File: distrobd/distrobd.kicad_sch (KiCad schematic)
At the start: 91 parts, among them J1 Conn_01x01, J10 Conn_01x01, J11 Conn_01x01, J12 Conn_02x03_Odd_Even, J13 Conn_02x03_Odd_Even, J14 Conn_02x03_Odd_Even, J15 Conn_02x03_Odd_Even, J16 Conn_01x01, J17 Conn_01x01, J18 Conn_02x03_Odd_Even, J19 Conn_02x03_Odd_Even, J2 Conn_01x01, J20 Conn_01x01, J21 Conn_01x01, J22 Conn_02x03_Odd_Even, J23 Conn_02x03_Odd_Even, J24 Conn_01x01, J25 Conn_01x01, J26 Conn_02x03_Odd_Even, J27 Conn_02x03_Odd_Even, J28 Conn_01x01, J29 Conn_01x01, J3 Conn_01x14, J30 Conn_02x03_Odd_Even, J31 Conn_02x03_Odd_Even, J32 Conn_01x01, J33 Conn_01x01, J34 Conn_02x03_Odd_Even, J35 Conn_02x03_Odd_Even, J36 Conn_01x01, J37 Conn_01x01, J38 Conn_02x03_Odd_Even, J39 Conn_02x03_Odd_Even, J4 Conn_01x14, J40 Conn_01x01, J41 Conn_01x01, J42 Conn_02x03_Odd_Even, J43 Conn_02x03_Odd_Even, J44 Conn_01x01, J45 Conn_01x01, J46 Conn_01x01, J47 Conn_01x01, J48 Conn_01x01, J49 Conn_01x01, J5 Conn_01x01, J50 Conn_01x01, J51 Conn_01x01, J6 Conn_01x01, J7 Conn_01x06, J8 Conn_01x06, J9 Conn_01x08

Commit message: minor touchups
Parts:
- added J52: Conn_01x04, Connector_Harwin:Harwin_M20-89004xx_1x04_P2.54mm_Horizontal, symbol Connector_Generic:Conn_01x04
- added JP3, JP4: SolderJumper_2_Bridged, Jumper:SolderJumper-2_P1.3mm_Bridged_RoundedPad1.0x1.5mm, symbol Jumper:SolderJumper_2_Bridged
- added R1, R2, R3, R4: 4k7, Resistor_SMD:R_1206_3216Metric_Pad1.30x1.75mm_HandSolder, symbol Device:R_Small_US
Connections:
- net +5V: now also J52.3 (Pin_3)
- net DUINO_GND: now also J8.2 (Pin_2)
- net VA: now also R4.2
- net VB: now also R3.2
- net VC: now also R2.2
- net VD: now also R1.2
- net V_CGND: now also R1.1, R2.1, R3.1, R4.1
- net at J8.1 (Pin_1): now also J52.2 (Pin_2)
- net at J8.3 (Pin_3): now also JP3.2 (B)
- net at J8.4 (Pin_4): now also JP4.2 (B)
- net SDA3: now reaches J4.6 (Pin_6)
- net SDA3: now also JP4.1 (A)
- net SCL3: now reaches J4.7 (Pin_7)
- net SCL3: now also JP3.1 (A)
- no-connect marks 26 -> 22
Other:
- note added: "INTERLOCK"
- note added: "MCP4728"
- note removed: "MCP4728 analog"
- note removed: "MCP4728 digital"
- moved on the sheet: J7, J8, J9

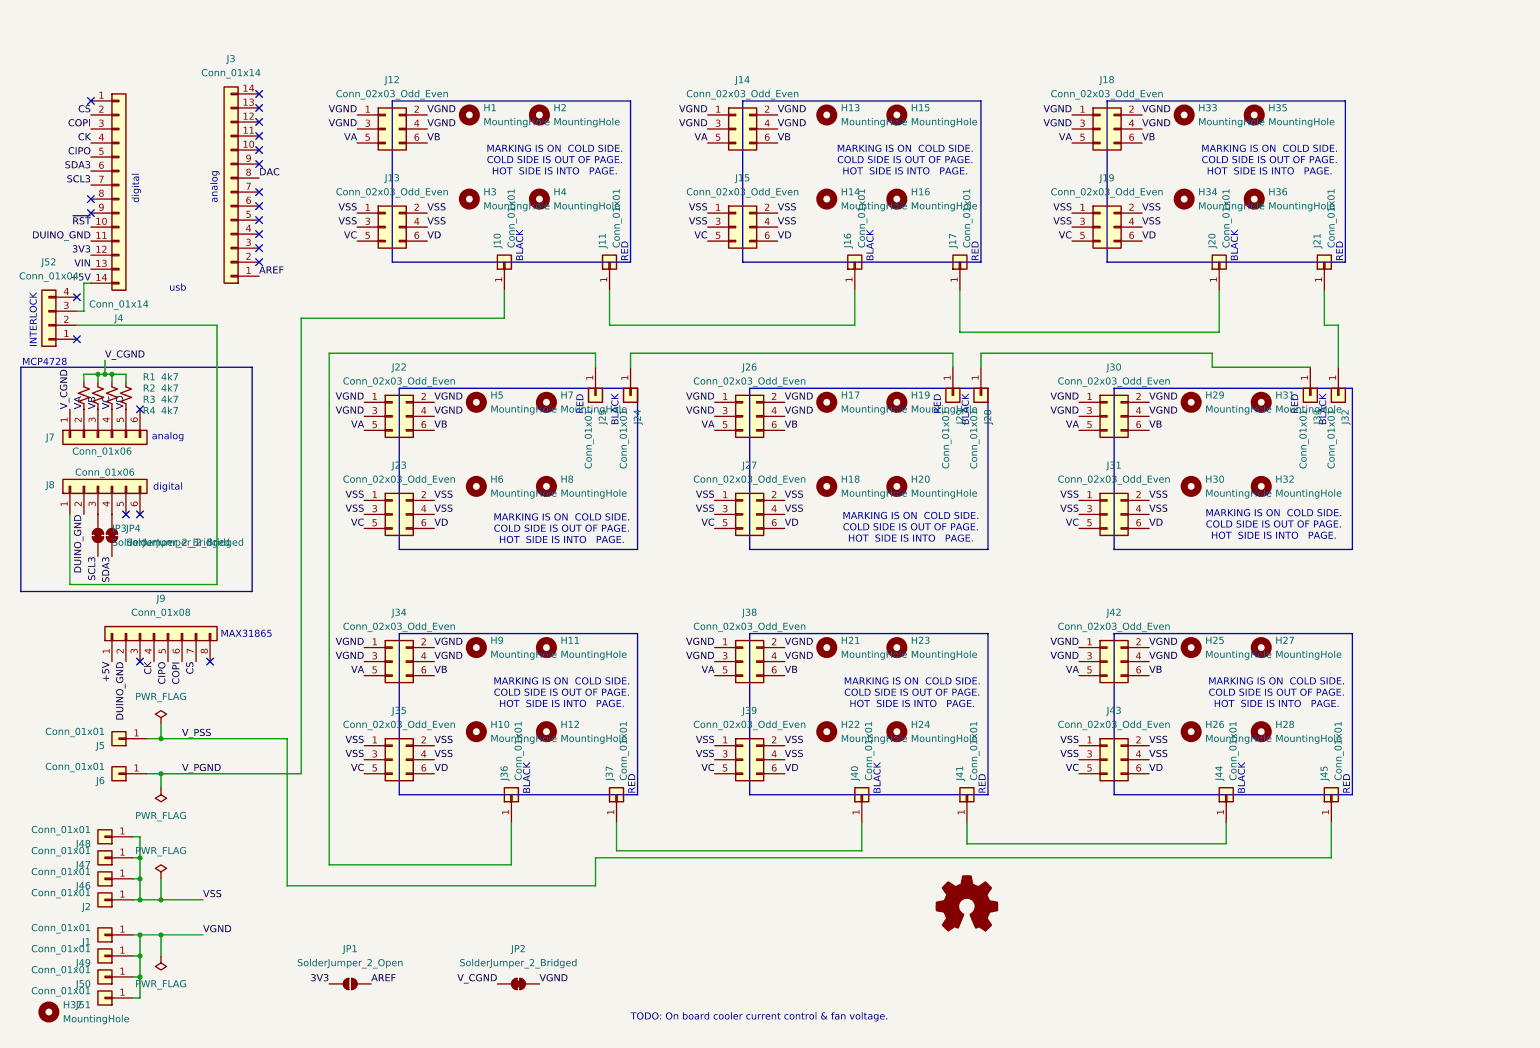
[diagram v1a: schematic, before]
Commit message: switch opamps to dual flavors, build in on-board TEC current control
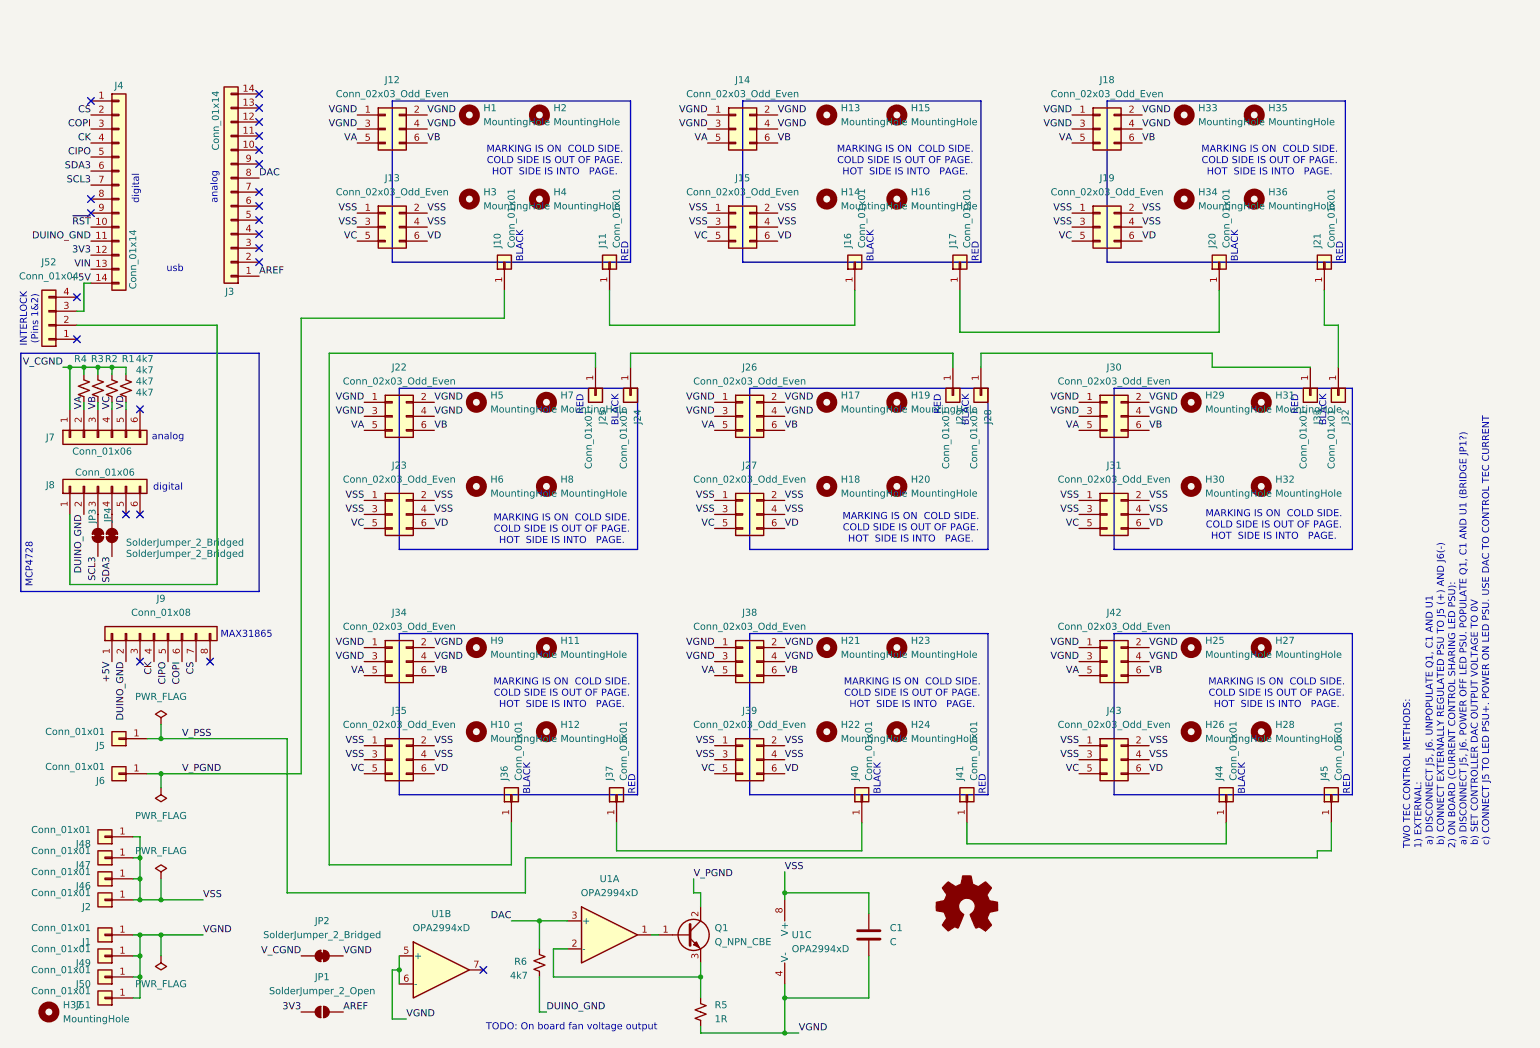
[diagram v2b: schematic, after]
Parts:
- added C1: C, Capacitor_SMD:C_0805_2012Metric_Pad1.18x1.45mm_HandSolder, symbol Device:C
- added Q1: Q_NPN_CBE, Package_TO_SOT_SMD:TO-252-2, symbol Transistor_BJT:Q_NPN_BCE
- added R5: 1R, Resistor_SMD:R_2512_6332Metric_Pad1.40x3.35mm_HandSolder, symbol Device:R_Small_US
- added R6: 4k7, Resistor_SMD:R_1206_3216Metric_Pad1.30x1.75mm_HandSolder, symbol Device:R_Small_US
- added U1: OPA2994xD, Package_SO:SOIC-8_3.9x4.9mm_P1.27mm, symbol Amplifier_Operational:OPA2994xD
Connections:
- net DAC: now also R6.1, U1.3 (+)
- net DUINO_GND: now also R6.2
- net VGND: now also C1.2, R5.2, U1.4 (V-), U1.5 (+), U1.6 (-)
- net VSS: now also C1.1, U1.8 (V+)
- net V_PGND: now also Q1.2 (C)
- new net: Q1.3 (E), R5.1, U1.2 (-)
- new net: Q1.1 (B), U1.1
- no-connect marks 22 -> 23
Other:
- note added: "INTERLOCK (Pins 1&2)"
- note added: "TODO: On board fan voltage output"
- note added: "TWO TEC CONTROL METHODS: 1) EXTERNAL: a) DISCONNECT J5, J6. UNPOPULATE Q1, C1 AND U1 b) CONNECT EXTERNALLY REGULATED PSU TO J5 (+) AND J6(-) 2) ON BOARD (CURRENT CONTROL SHARING LED PSU): a) DISCONNECT J5, J6. POWER OFF LED PSU. POPULATE Q1, C1 AND U1 (BRIDGE JP1?) b) SET CONTROLLER DAC OUTPUT VOLTAGE TO 0V c) CONNECT J5 TO LED PSU+. POWER ON LED PSU. USE DAC TO CONTROL TEC CURRENT"
- note removed: "INTERLOCK"
- note removed: "TODO: On board cooler current control & fan voltage."
- moved on the sheet: JP1, JP2, R1, R2, R3, R4

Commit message: rev up light
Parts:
- removed J46, J47, J48, J49, J50, J51, J6: Conn_01x01, custom:TE_2834012-3_1x01_P4.0mm_Horizontal, symbol Connector_Generic:Conn_01x01
- removed JP1: SolderJumper_2_Open, Jumper:SolderJumper-2_P1.3mm_Open_RoundedPad1.0x1.5mm, symbol Jumper:SolderJumper_2_Open
- removed JP2: SolderJumper_2_Bridged, Jumper:SolderJumper-2_P1.3mm_Bridged2Bar_RoundedPad1.0x1.5mm, symbol Jumper:SolderJumper_2_Bridged
- removed JP3, JP4: SolderJumper_2_Bridged, Jumper:SolderJumper-2_P1.3mm_Bridged_RoundedPad1.0x1.5mm, symbol Jumper:SolderJumper_2_Bridged
- added C2, C3: 0.1uF, Capacitor_SMD:C_0805_2012Metric_Pad1.18x1.45mm_HandSolder, symbol Device:C
- added J6: Conn_01x04, Connector_Harwin:Harwin_M20-89004xx_1x04_P2.54mm_Horizontal, symbol Connector_Generic:Conn_01x04
- added JP1, JP6, JP7, JP8: SolderJumper_2_Bridged, Jumper:SolderJumper-2_P1.3mm_Bridged2Bar_RoundedPad1.0x1.5mm, symbol Jumper:SolderJumper_2_Bridged
- added JP10, JP11, JP12, JP13, JP14, JP15, JP16, JP17, JP18, JP19, JP2, JP20, JP5, JP9: SolderJumper_2_Open, Jumper:SolderJumper-2_P1.3mm_Open_RoundedPad1.0x1.5mm, symbol Jumper:SolderJumper_2_Open
- added R10, R8: 0R, Resistor_SMD:R_1206_3216Metric_Pad1.30x1.75mm_HandSolder, symbol Device:R_Small_US
- added R7: 100K, Resistor_SMD:R_1206_3216Metric_Pad1.30x1.75mm_HandSolder, symbol Device:R_Small_US
- added U2, U3: OPA2994xD, Package_SO:SOIC-8_3.9x4.9mm_P1.27mm, symbol Amplifier_Operational:OPA2994xD
- added U4: NCS1S2412SC, Converter_DCDC:Converter_DCDC_Murata_NCS1SxxxxSC_THT, symbol Converter_DCDC:NCS1S2412SC
- C1: value C -> 0.1uF
- R5: value 1R -> 2R
- R6: value 4k7 -> 2R; footprint Resistor_SMD:R_1206_3216Metric_Pad1.30x1.75mm_HandSolder -> Resistor_SMD:R_2512_6332Metric_Pad1.40x3.35mm_HandSolder
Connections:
- net V_CGND is gone; now on net GND: J7.1 (Pin_1), R1.1, R2.1, R3.1, R4.1
- net 3V3: now also JP1.1 (A)
- net AREF: now also JP1.2 (B)
- net SCL3: now also J8.3 (Pin_3)
- net SDA3: now also J8.4 (Pin_4)
- net VA: now also JP14.2 (B), U2.1, U2.2 (-); no longer J7.2 (Pin_2), R4.2
- net VB: now also JP15.2 (B), U2.6 (-), U2.7; no longer J7.3 (Pin_3), R3.2
- net VC: now also JP16.2 (B), U3.1, U3.2 (-); no longer J7.4 (Pin_4), R2.2
- net VD: now also JP17.2 (B), U3.6 (-), U3.7; no longer J7.5 (Pin_5), R1.2
- net +5V_LOCK: now reaches J52.2 (Pin_2), J8.1 (Pin_1)
- net +5V_LOCK: now also J7.6 (Pin_6)
- net at U1.7: now also U1.6 (-), JP7.1 (A)
- net at Q1.3 (E), R5.1, U1.2 (-): now also R6.1
- net FAN_TACH: now reaches J3.13 (Pin_13)
- net FAN_TACH: now also R10.2
- net FAN_PWM: now reaches J3.14 (Pin_14)
- net FAN_PWM: now also R8.2
- removed net DAC: J3.8 (Pin_8), R6.1, U1.3 (+)
- net DUINO_GND renamed GND
- net GND: now also C1.2, J1.1 (Pin_1), J13.1 (Pin_1), J13.2 (Pin_2), J13.3 (Pin_3), J13.4 (Pin_4), J15.1 (Pin_1), J15.2 (Pin_2), J15.3 (Pin_3), J15.4 (Pin_4), J19.1 (Pin_1), J19.2 (Pin_2), J19.3 (Pin_3), J19.4 (Pin_4), J23.1 (Pin_1), J23.2 (Pin_2), J23.3 (Pin_3), J23.4 (Pin_4), J27.1 (Pin_1), J27.2 (Pin_2), J27.3 (Pin_3), J27.4 (Pin_4), J31.1 (Pin_1), J31.2 (Pin_2), J31.3 (Pin_3), J31.4 (Pin_4), J35.1 (Pin_1), J35.2 (Pin_2), J35.3 (Pin_3), J35.4 (Pin_4), J39.1 (Pin_1), J39.2 (Pin_2), J39.3 (Pin_3), J39.4 (Pin_4), J43.1 (Pin_1), J43.2 (Pin_2), J43.3 (Pin_3), J43.4 (Pin_4), R5.2, U1.4 (V-), C2.2, C3.2, JP10.2 (B), JP18.2 (B), JP2.2 (B), JP20.1 (A), JP9.2 (B), R7.1, U2.4 (V-), U3.4 (V-), U4.1 (-VIN)
- net VGND renamed VLED
- net VLED: now also J2.1 (Pin_1), C2.1, C3.1, JP11.1 (A), JP12.1 (A), JP13.1 (A), JP8.2 (B), U2.8 (V+), U3.8 (V+); no longer C1.2, J1.1 (Pin_1), R5.2, U1.4 (V-), U1.5 (+), U1.6 (-)
- removed net VSS: C1.1, J13.1 (Pin_1), J13.2 (Pin_2), J13.3 (Pin_3), J13.4 (Pin_4), J15.1 (Pin_1), J15.2 (Pin_2), J15.3 (Pin_3), J15.4 (Pin_4), J19.1 (Pin_1), J19.2 (Pin_2), J19.3 (Pin_3), J19.4 (Pin_4), J2.1 (Pin_1), J23.1 (Pin_1), J23.2 (Pin_2), J23.3 (Pin_3), J23.4 (Pin_4), J27.1 (Pin_1), J27.2 (Pin_2), J27.3 (Pin_3), J27.4 (Pin_4), J31.1 (Pin_1), J31.2 (Pin_2), J31.3 (Pin_3), J31.4 (Pin_4), J35.1 (Pin_1), J35.2 (Pin_2), J35.3 (Pin_3), J35.4 (Pin_4), J39.1 (Pin_1), J39.2 (Pin_2), J39.3 (Pin_3), J39.4 (Pin_4), J43.1 (Pin_1), J43.2 (Pin_2), J43.3 (Pin_3), J43.4 (Pin_4), U1.8 (V+)
- net V_PGND renamed VTEC_LO
- net VTEC_LO: now also JP10.1 (A), JP2.1 (A), JP9.1 (A)
- net V_PSS renamed VTEC
- net VTEC: now also C1.1, U1.8 (V+), JP11.2 (B), JP12.2 (B), JP13.2 (B), JP19.2 (B)
- new net: J6.3 (Pin_3), R10.1
- new net: J6.4 (Pin_4), R8.1
- new net: JP5.1 (A), JP7.2 (B), U1.3 (+)
- new net: JP19.1 (A), JP8.1 (A), U4.2 (+VIN)
- new net: JP18.1 (A), JP6.2 (B), U1.5 (+)
- new net 12V_FAN_POWER: J6.2 (Pin_2), U4.6 (+VOUT)
- new net FAN_GND: J6.1 (Pin_1), JP20.2 (B), U4.7 (-VOUT)
- new net TEC_DAC: J3.8 (Pin_8), JP5.2 (B), JP6.1 (A), R7.2
- new net VAR: J7.2 (Pin_2), JP14.1 (A), R4.2, U2.3 (+)
- new net VBR: J7.3 (Pin_3), JP15.1 (A), R3.2, U2.5 (+)
- new net VCR: J7.4 (Pin_4), JP16.1 (A), R2.2, U3.3 (+)
- new net VDR: J7.5 (Pin_5), JP17.1 (A), R1.2, U3.5 (+)
- no-connect marks 23 -> 22
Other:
- note added: "BRIDGE THESE TO USE LED POWER FOR TEC"
- note added: "H7 USB HERE (for upside-down mount)"
- note added: "INTERLOCK (Pins 2&3)"
- note added: "TEC SUPPLY OPTIONS: 1) EXTERNAL CONTROL: a) DNP U1, Q1, R5/R6, C1 (UNBRIDGE J1) b) BRIDGE JP2, JP9, JP10 c) UNBRIDGE, JP11, JP12, JP13 d) CONNECT EXTERNALLY REGULATED TEC PSU TO J5 (+) AND J1(-) 2) ON-BOARD CONTROL: a) SEPARATE TEC AND LED VOLTAGE SOURCES I) POPULATE U1, Q1, C1, R5/R6, BRIDGE J1 II) UNBRIDGE JP2, JP9, JP10 III) UNBRIDGE, JP11, JP12, JP13 IV) CONNECT TEC VOLTAGE SOURCE TO J5 (+) A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"
- note removed: "INTERLOCK (Pins 1&2)"
- note removed: "TODO: On board fan voltage output"
- note removed: "TWO TEC CONTROL METHODS: 1) EXTERNAL: a) DISCONNECT J5, J6. UNPOPULATE Q1, C1 AND U1 b) CONNECT EXTERNALLY REGULATED PSU TO J5 (+) AND J6(-) 2) ON BOARD (CURRENT CONTROL SHARING LED PSU): a) DISCONNECT J5, J6. POWER OFF LED PSU. POPULATE Q1, C1 AND U1 (BRIDGE JP1?) b) SET CONTROLLER DAC OUTPUT VOLTAGE TO 0V c) CONNECT J5 TO LED PSU+. POWER ON LED PSU. USE DAC TO CONTROL TEC CURRENT"
- note removed: "usb"
- moved on the sheet: C1, H37, J1, J2, J3, J4, J5, J52, J7, J8, J9, Q1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

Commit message: rev up light
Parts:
- removed J3, J4: Conn_01x14, Connector_PinSocket_2.54mm:PinSocket_1x14_P2.54mm_Vertical_SMD_Pin1Left, symbol Connector_Generic:Conn_01x14
- added H38, H39: MountingHole, MountingHole:MountingHole_2.2mm_M2, symbol Mechanical:MountingHole
- added H40, H41, H42, H43: MountingHole, custom:13.5mm_NPTH, symbol Mechanical:MountingHole
- added J46, J47: Conn_02x14_Top_Bottom, Connector_PinSocket_2.54mm:PinSocket_2x14_P2.54mm_Vertical_SMD, symbol Connector_Generic:Conn_02x14_Odd_Even
- J1, J2, J5: footprint custom:TE_2834012-3_1x01_P4.0mm_Horizontal -> custom:LF994006
- J6: footprint Connector_Harwin:Harwin_M20-89004xx_1x04_P2.54mm_Horizontal -> Connector:FanPinHeader_1x04_P2.54mm_Vertical
- JP1, JP6, JP7: footprint Jumper:SolderJumper-2_P1.3mm_Bridged2Bar_RoundedPad1.0x1.5mm -> Jumper:SolderJumper-2_P1.3mm_Bridged_RoundedPad1.0x1.5mm
- R6: footprint Resistor_SMD:R_2512_6332Metric_Pad1.40x3.35mm_HandSolder -> Package_TO_SOT_SMD:TO-263-2_TabPin1
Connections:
- net +5V: now also J46.27 (Pin_27), J46.28 (Pin_28)
- net 3V3: now also J46.23 (Pin_23), J46.24 (Pin_24)
- net AREF: now also J47.1 (Pin_1), J47.2 (Pin_2)
- net CIPO: now also J46.10 (Pin_10), J46.9 (Pin_9)
- net CK: now also J46.7 (Pin_7), J46.8 (Pin_8)
- net COPI: now also J46.5 (Pin_5), J46.6 (Pin_6)
- net CS: now also J46.3 (Pin_3), J46.4 (Pin_4)
- net FAN_PWM: now also J47.27 (Pin_27), J47.28 (Pin_28)
- net FAN_TACH: now also J47.25 (Pin_25), J47.26 (Pin_26)
- net GND: now also J46.21 (Pin_21), J46.22 (Pin_22)
- net SCL3: now also J46.13 (Pin_13), J46.14 (Pin_14)
- net SDA3: now also J46.11 (Pin_11), J46.12 (Pin_12)
- net TEC_DAC: now also J47.15 (Pin_15), J47.16 (Pin_16)
- net VIN: now also J46.25 (Pin_25), J46.26 (Pin_26)
- net ~{RST}: now also J46.19 (Pin_19), J46.20 (Pin_20)
- new net: J46.1 (Pin_1), J46.2 (Pin_2)
- new net: J46.15 (Pin_15), J46.16 (Pin_16)
- new net: J46.17 (Pin_17), J46.18 (Pin_18)
- new net: J47.10 (Pin_10), J47.9 (Pin_9)
- new net: J47.11 (Pin_11), J47.12 (Pin_12)
- new net: J47.13 (Pin_13), J47.14 (Pin_14)
- new net: J47.17 (Pin_17), J47.18 (Pin_18)
- new net: J47.19 (Pin_19), J47.20 (Pin_20)
- new net: J47.21 (Pin_21), J47.22 (Pin_22)
- new net: J47.23 (Pin_23), J47.24 (Pin_24)
- new net: J47.3 (Pin_3), J47.4 (Pin_4)
- new net: J47.5 (Pin_5), J47.6 (Pin_6)
- new net: J47.7 (Pin_7), J47.8 (Pin_8)
- no-connect marks 22 -> 7
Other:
- moved on the sheet: J9, JP19, JP20, JP8, R7, U4
